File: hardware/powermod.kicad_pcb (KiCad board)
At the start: 4 copper layers, 65 x 40 mm, 77 parts, among them J1 USB_C_IN, J2 USB_C_OUT, J3 JST_PH_2, J4 STEMMA_QT, J5 UPDI_HDR, Q1 AON7407, Q2 AON7407, Q3 BSS138, SW1 BUTTON, U1 BM8563, U2 ATtiny1616, U3 TPS63020DSJR, U4 TP4056, U5 XC6206P332MR, Y1 32.768kHz

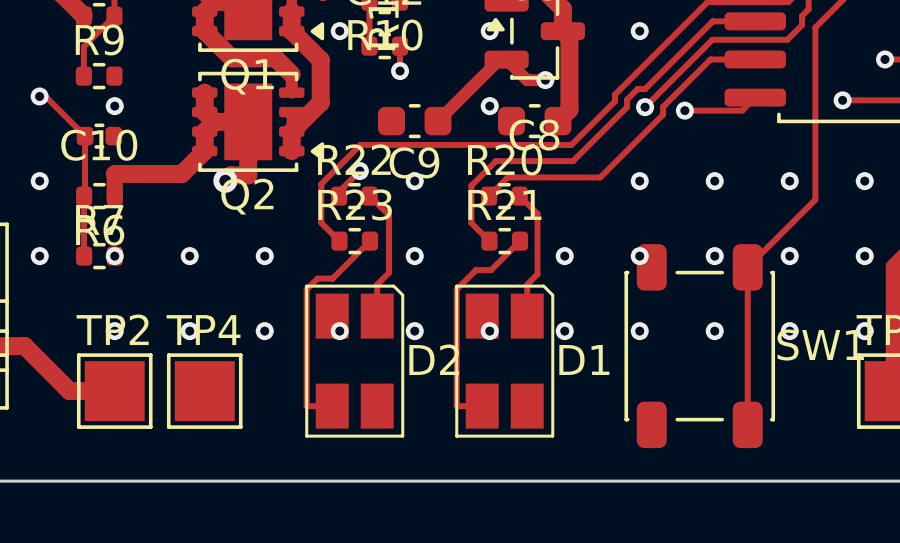
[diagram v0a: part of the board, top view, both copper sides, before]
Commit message: hardware: commit LED + crystal BOM parts (both in-stock, verified)
Crystal Y1: Epson Q13FC13500004 (LCSC C32346, ~286k stock) — 32.768kHz
CL=12.5pF matching the BM8563. Netlist-only (footprint unchanged).

LEDs D1/D2: TOGIALED TJ-S3227 (LCSC C601677, ~7.7k stock), yellow-green die
fixes the dim-green issue. Its pinout is the OPPOSITE numbering to the stock
KiCad Avago PLCC4 (would reverse polarity), so a local footprint was built
from LCSC's EasyEDA model (2 independent diodes, anodes=pins 2/3,
cathodes=pins 1/4). D1/D2 swapped on the board and anodes re-routed; cathodes
tie through the GND pour. Board rebuilt at rot 0 (anodes stacked under the
resistors, no crossing). LED_SMD lib dropped (both LEDs now in powermod lib).

Verified: pad-diff 214/214 + 11 NC, 0 unconnected, 0 clearance, only the 4
intrinsic U3 QFN-neck track_width flags. Red/green die identity is
firmware-adjustable (documented in PREFAB_AUDIT.md).

Co-Authored-By: Claude Opus 4.8 <noreply@anthropic.com>
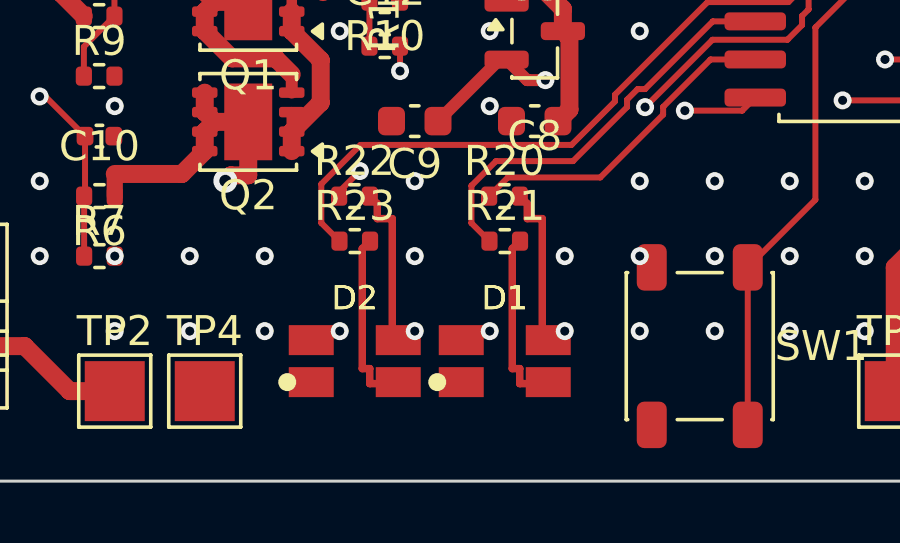
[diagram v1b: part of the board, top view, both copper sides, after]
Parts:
- D1, D2: value LED_RG_PLCC4 -> TJ-S3227; footprint LED_Avago_PLCC4_3.2x2.8mm_CW -> LED_TJ-S3227_RG_3.2x2.7mm
- turned D1 to 0 degrees
- turned D2 to 0 degrees
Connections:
- D1 pad 1: D1_RED -> GND
- D1 pad 2: GND -> D1_GRN
- D1 pad 3: D1_GRN -> D1_RED
- D2 pad 1: D2_RED -> GND
- D2 pad 2: GND -> D2_GRN
- D2 pad 3: D2_GRN -> D2_RED
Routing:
- net D2_GRN: track 7.52 -> 6.18 mm
- net D1_GRN: track 7.52 -> 6.18 mm
- net D1_RED: track 4.39 -> 5.67 mm, vias 0 -> 1
- net D2_RED: track 4.43 -> 5.67 mm, vias 0 -> 1
- net GND: vias 151 -> 149

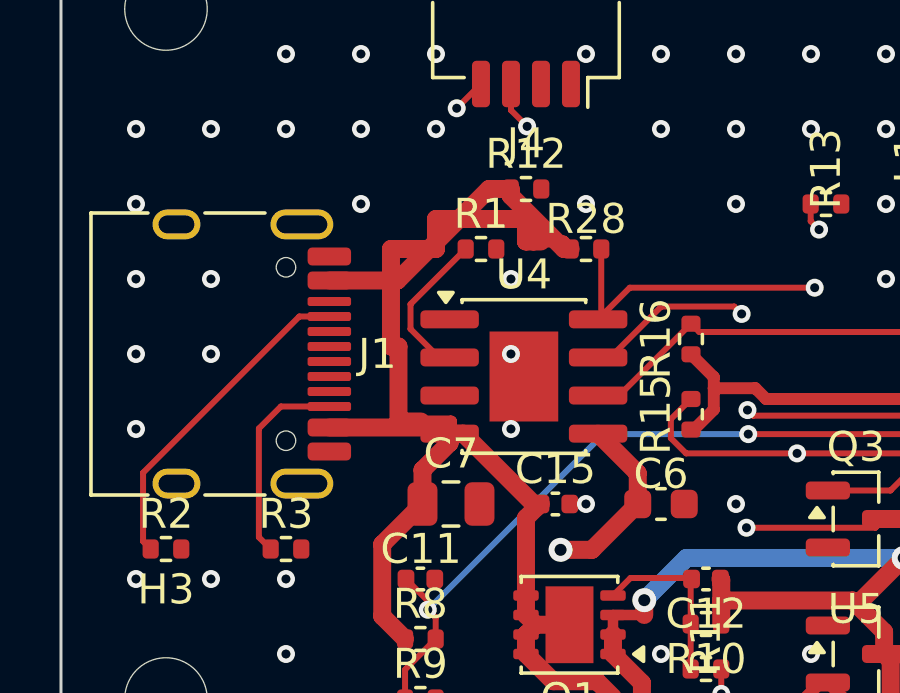
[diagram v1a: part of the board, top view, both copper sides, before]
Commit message: hardware: VBUS current-sharing (manual route) + audit review pass
VBUS current-sharing (audit open item d): A4↔A9 tied with a 0.6mm F.Cu link
in the narrow channel right of the connector pad column — routed by hand in
KiCad where the scripts could only fit 0.4mm. Split is now A9 73% / A4 27%
(was ~100/0): A9's USB-C contacts drop from 1.15A to 0.84A each at the 2.3A
peak, comfortably inside the ~1.25A/contact rating. Also simplified several
VBUS/other routes in passing.

Audit review pass on PREFAB_AUDIT.md: fixed stale counts (214/214 pads, 234
SMD pads); rewrote the ADC-reference firmware note (use VDD/3.3V or 2.5V, not
the marginal 1.5V); added Finding 3 (power-rail width-vs-current analysis) and
the U3 EP via-tenting fab note.

Verified: pad-diff 214/214 + 11 NC, 0 unconnected, 0 clearance, all rails at
spec (only the 4 intrinsic U3 QFN-neck track_width flags).

Co-Authored-By: Claude Opus 4.8 <noreply@anthropic.com>
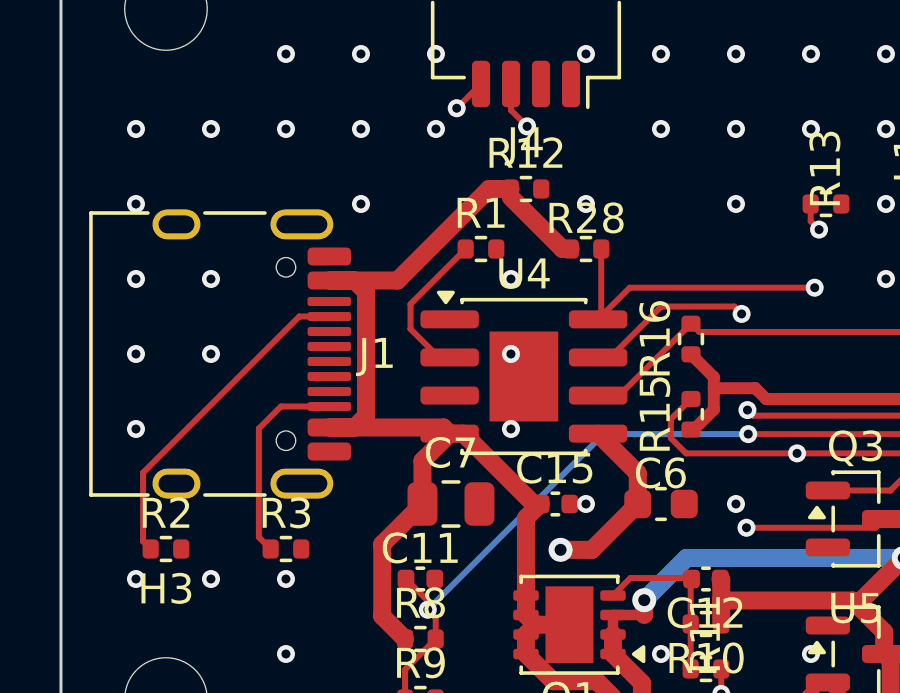
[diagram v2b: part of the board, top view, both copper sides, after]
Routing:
- net VBUS: track 53.3 -> 43.8 mm
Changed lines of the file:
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@@
-	)
-	(segment
-		(start 12.5 11.5)
-		(end 12.5 10.5)
-		(width 0.6)
-		(layer "F.Cu")
-		(net "VBUS")
-	)
-	(segment
-		(start 15.75 11.25)
-		(end 16 11.25)
-		(width 0.6)
-		(layer "F.Cu")
-		(net "VBUS")
-	)
-	(segment
-		(start 12 17.25)
-		(end 11.25 17.25)
-		(width 0.6)
-		(layer "F.Cu")
-		(net "VBUS")
 	)
 	(segment
@@
 	)
 	(segment
-		(start 16.75 11.25)
-		(end 16.99 11.5)
-		(width 0.4)
-		(layer "F.Cu")
-		(net "VBUS")
-	)
-	(segment
-		(start 15.5 10.5)
-		(end 15.5 11.25)
-		(width 0.6)
-		(layer "F.Cu")
-		(net "VBUS")
-	)
-	(segment
-		(start 16 11.25)
-		(end 16.75 11.25)
-		(width 0.4)
-		(layer "F.Cu")
-		(net "VBUS")
-	)
-	(segment
-		(start 12.955 17.655)
-		(end 12.955 17.9616)
-		(width 0.6)
-		(layer "F.Cu")
-		(net "VBUS")
-	)
-	(segment
 		(start 16.4083 25.9083)
 		(end 15.5 25)
@@
 	)
 	(segment
-		(start 12.5 10.5)
-		(end 15.5 10.5)
-		(width 0.6)
-		(layer "F.Cu")
-		(net "VBUS")
-	)
-	(segment
 		(start 15.825 24.025)
 		(end 15.5 23.7)
@@
 	)
 	(segment
-		(start 11 14.75)
-		(end 11 11.5)
-		(width 0.6)
-		(layer "F.Cu")
-		(net "VBUS")
-	)
-	(segment
 		(start 15.862 20.1032)
 		(end 15.9652 20)
@@
 	)
 	(segment
-		(start 13 17.25)
-		(end 12 17.25)
-		(width 0.4)
-		(layer "F.Cu")
-		(net "VBUS")
-	)
-	(segment
-		(start 11.25 14.75)
-		(end 11 14.75)
+		(start 9.785252 12.55)
+		(end 10.17 12.934748)
+		(width 0.6)
+		(layer "F.Cu")
+		(net "VBUS")
+	)
+	(segment
+		(start 12.05 18.56)
+		(end 12.955 17.655)
+		(width 0.6)
+		(layer "F.Cu")
+		(net "VBUS")
+	)
+	(segment
+		(start 16.99 11.5)
+		(end 16.720001 11.5)
 		(width 0.6)
 		(layer "F.Cu")
@@
 	)
 	(segment
+		(start 9.785252 17.45)
+		(end 8.945 17.45)
+		(width 0.6)
+		(layer "F.Cu")
+		(net "VBUS")
+	)
+	(segment
 		(start 14.268232 9.5)
 		(end 14.99 9.5)
@@
 	)
 	(segment
+		(start 10.17 17.065252)
+		(end 9.785252 17.45)
+		(width 0.6)
+		(layer "F.Cu")
+		(net "VBUS")
+	)
+	(segment
 		(start 11.218232 12.55)
 		(end 14.268232 9.5)
@@
 	)
 	(segment
+		(start 16.720001 11.5)
+		(end 14.99 9.769999)
+		(width 0.6)
+		(layer "F.Cu")
+		(net "VBUS")
+	)
+	(segment
+		(start 12.05 20)
+		(end 12.05 18.56)
+		(width 0.6)
+		(layer "F.Cu")
+		(net "VBUS")
+	)
+	(segment
 		(start 13.4138 17.655)
 		(end 12.955 17.655)
@@
 	)
 	(segment
-		(start 16.7667 11.5)
-		(end 14.99 9.7233)
-		(width 0.6)
-		(layer "F.Cu")
-		(net "VBUS")
-	)
-	(segment
-		(start 13 17.75)
-		(end 13 17.25)
-		(width 0.4)
-		(layer "F.Cu")
-		(net "VBUS")
-	)
-	(segment
 		(start 11.47 24.5)
 		(end 10.7074 23.7374)
@@
 	)
 	(segment
-		(start 11.25 17.25)
-		(end 11.25 14.75)
-		(width 0.6)
-		(layer "F.Cu")
-		(net "VBUS")
-	)
-	(segment
 		(start 8.945 17.45)
 		(end 12.75 17.45)
@@
 		(start 8.945 12.55)
 		(end 11.218232 12.55)
-		(width 0.6)
-		(layer "F.Cu")
-		(net "VBUS")
-	)
-	(segment
-		(start 14.99 9.7233)
-		(end 14.99 9.5)
 		(width 0.6)
 		(layer "F.Cu")
@@
 	)
 	(segment
-		(start 16.99 11.5)
-		(end 16.7667 11.5)
-		(width 0.6)
-		(layer "F.Cu")
-		(net "VBUS")
-	)
-	(segment
-		(start 11 11.5)
-		(end 12.5 11.5)
+		(start 10.17 12.934748)
+		(end 10.17 17.065252)
 		(width 0.6)
 		(layer "F.Cu")
@@
 	)
 	(segment
-		(start 12.955 17.9616)
-		(end 12.05 18.8666)
+		(start 8.945 12.55)
+		(end 9.785252 12.55)
 		(width 0.6)
 		(layer "F.Cu")
@@
 		(start 10.7074 23.7374)
 		(end 10.7074 21.3426)
-		(width 0.6)
-		(layer "F.Cu")
-		(net "VBUS")
-	)
-	(segment
-		(start 15.5 11.25)
-		(end 15.75 11.25)
-		(width 0.6)
-		(layer "F.Cu")
-		(net "VBUS")
-	)
-	(segment
-		(start 12.96 17.66)
-		(end 13 17.75)
-		(width 0.4)
-		(layer "F.Cu")
-		(net "VBUS")
-	)
-	(segment
-		(start 12.05 18.8666)
-		(end 12.05 20)
 		(width 0.6)
 		(layer "F.Cu")
@@
 	)
 	(segment
+		(start 21 36.25)
+		(end 20.75 36.25)
+		(width 0.25)
+		(layer "F.Cu")
+		(net "D2_GRN")
+	)
+	(segment
+		(start 22 36.75)
+		(end 21 36.75)
+		(width 0.25)
+		(layer "F.Cu")
+		(net "D2_GRN")
+	)
+	(segment
+		(start 20.75 32.25)
+		(end 21.01 32)
+		(width 0.25)
+		(layer "F.Cu")
+		(net "D2_GRN")
+	)
+	(segment
+		(start 21 36.75)
+		(end 21 36.25)
+		(width 0.25)
+		(layer "F.Cu")
+		(net "D2_GRN")
+	)
+	(segment
+		(start 20.75 36.25)
+		(end 20.75 32.25)
+		(width 0.25)
+		(layer "F.Cu")
+		(net "D2_GRN")
+	)
+	(segment
+		(start 21.95 36.7)
+		(end 22 36.75)
+		(width 0.25)
+		(layer "F.Cu")
+		(net "D2_GRN")
+	)
+	(segment
 		(start 25.6022 29.8778)
 		(end 28.6848 29.8778)
@@
 		(net "Q3_DRAIN")
 	)
-	(segment
-		(start 21 36.25)
-		(end 20.75 36.25)
-		(width 0.25)
-		(layer "F.Cu")
-		(net "D2_GRN")
-	)
-	(segment
-		(start 22 36.75)
-		(end 21 36.75)
-		(width 0.25)
-		(layer "F.Cu")
-		(net "D2_GRN")
-	)
-	(segment
-		(start 20.75 32.25)
-		(end 21.01 32)
-		(width 0.25)
-		(layer "F.Cu")
-		(net "D2_GRN")
-	)
-	(segment
-		(start 21 36.75)
-		(end 21 36.25)
-		(width 0.25)
-		(layer "F.Cu")
-		(net "D2_GRN")
-	)
-	(segment
-		(start 20.75 36.25)
-		(end 20.75 32.25)
-		(width 0.25)
-		(layer "F.Cu")
-		(net "D2_GRN")
-	)
-	(segment
-		(start 21.95 36.7)
-		(end 22 36.75)
-		(width 0.25)
-		(layer "F.Cu")
-		(net "D2_GRN")
-	)
 	(zone

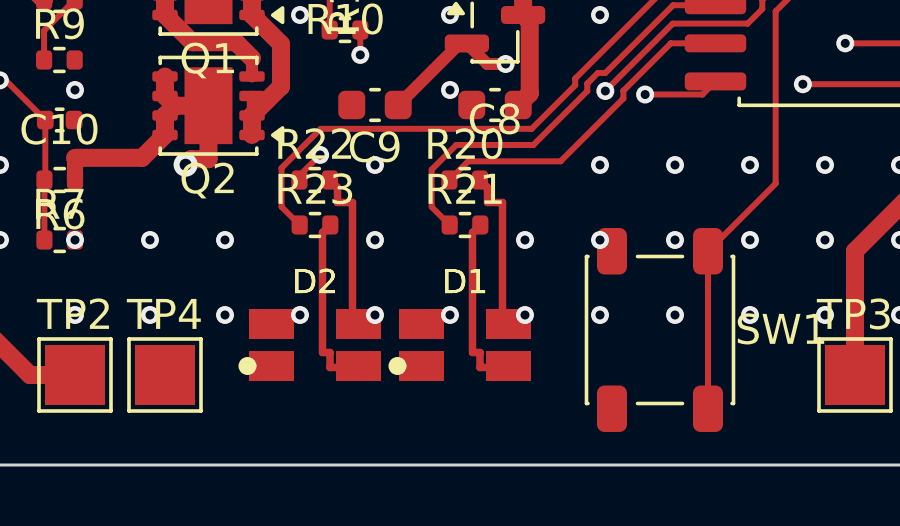
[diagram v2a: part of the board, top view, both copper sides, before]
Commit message: hardware: gerber review — remove 2 dangling vias on D1_RED/D2_RED
Fab-review pass: exported full gerber+drill set and checked manufacturing
minimums (all inside JLCPCB standard: 0.2mm trace/space, 0.6/0.3 vias =
0.15mm ring, 0.3mm min drill, 0.225mm min PTH ring). DRC clean except
cosmetic silk + the 4 intrinsic U3 QFN necks.

Found and removed 2 dangling vias (redundant single-layer stubs on the LED
red-anode nets at (22.5,35)/(27.5,35)) left over from LED-area routing.
Verified: 0 unconnected, pad-diff still 214/214.

Co-Authored-By: Claude Opus 4.8 <noreply@anthropic.com>
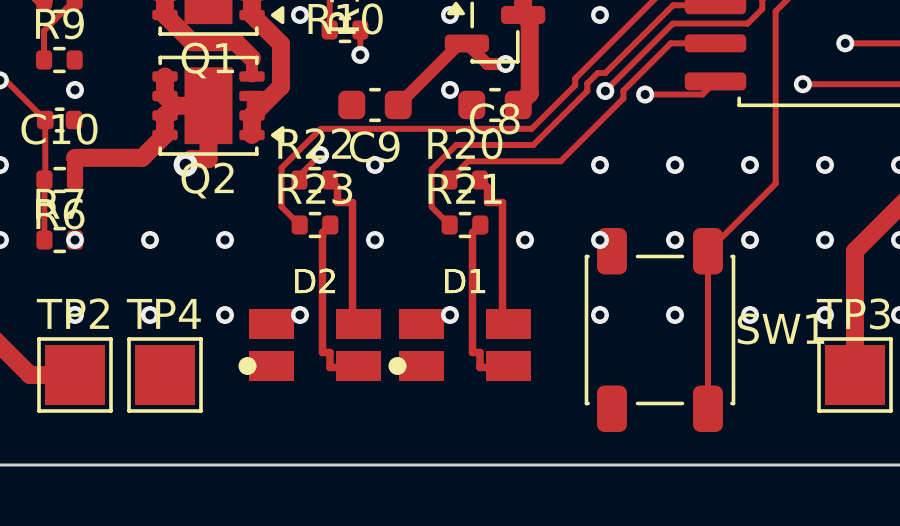
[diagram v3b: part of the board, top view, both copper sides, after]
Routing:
- net D2_RED: vias 1 -> 0
- net D1_RED: vias 1 -> 0
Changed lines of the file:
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@@
-		(net "D2_RED")
-	)
-	(via
-		(at 22.5 35)
-		(size 0.6)
-		(drill 0.3)
-		(layers "F.Cu" "B.Cu")
 		(net "D2_RED")
 	)
@@
 		(net "D1_RED")
 	)
-	(via
-		(at 27.5 35)
-		(size 0.6)
-		(drill 0.3)
-		(layers "F.Cu" "B.Cu")
-		(net "D1_RED")
-	)

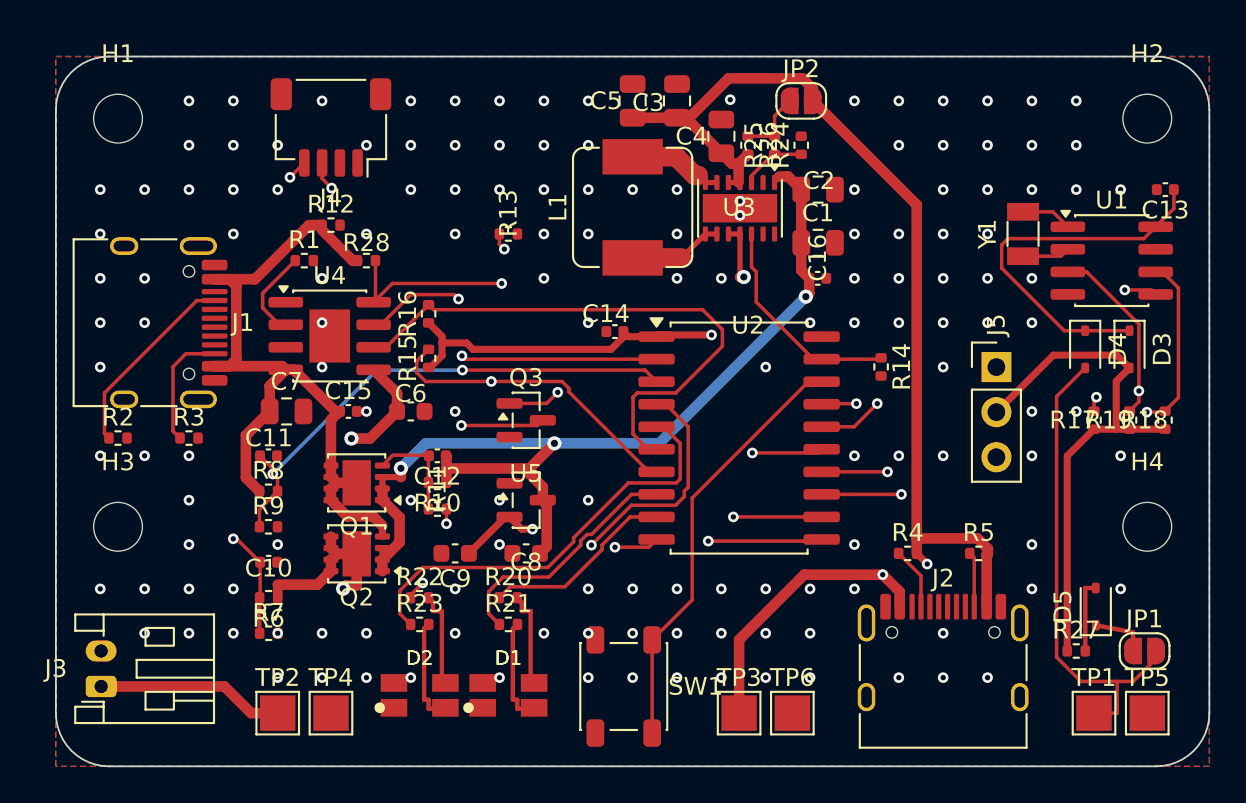
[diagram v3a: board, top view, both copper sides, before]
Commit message: hardware: board footprint swap for PY32F003 (U2 TSSOP-20, J5 SWD, TP7 NRST)
Text-level swap on powermod.kicad_pcb (pcbnew footprint mutation segfaults):
- U2 SOIC-20W -> TSSOP-20_4.4x6.5mm, 20 pads net-assigned to the PY32 pinmap
- J5 3-pin UPDI -> 3-pin SWD (GND/SWCLK/SWDIO); a 5-pin header won't fit the
  packed RTC/USB corner, so NRST is exposed on the new TP7 probe pad instead
- stripped 201 stale MCU-net segments + 6 local 3V3/GND stubs
Verified in pcbnew: correct nets, zero courtyard collisions. DRC clean apart
from the 4 known U3 track_width necks + 36 unrouted MCU connections (ratsnest).
MCU-area routing still to do; power/USB/charger routing untouched.

Co-Authored-By: Claude Opus 4.8 <noreply@anthropic.com>
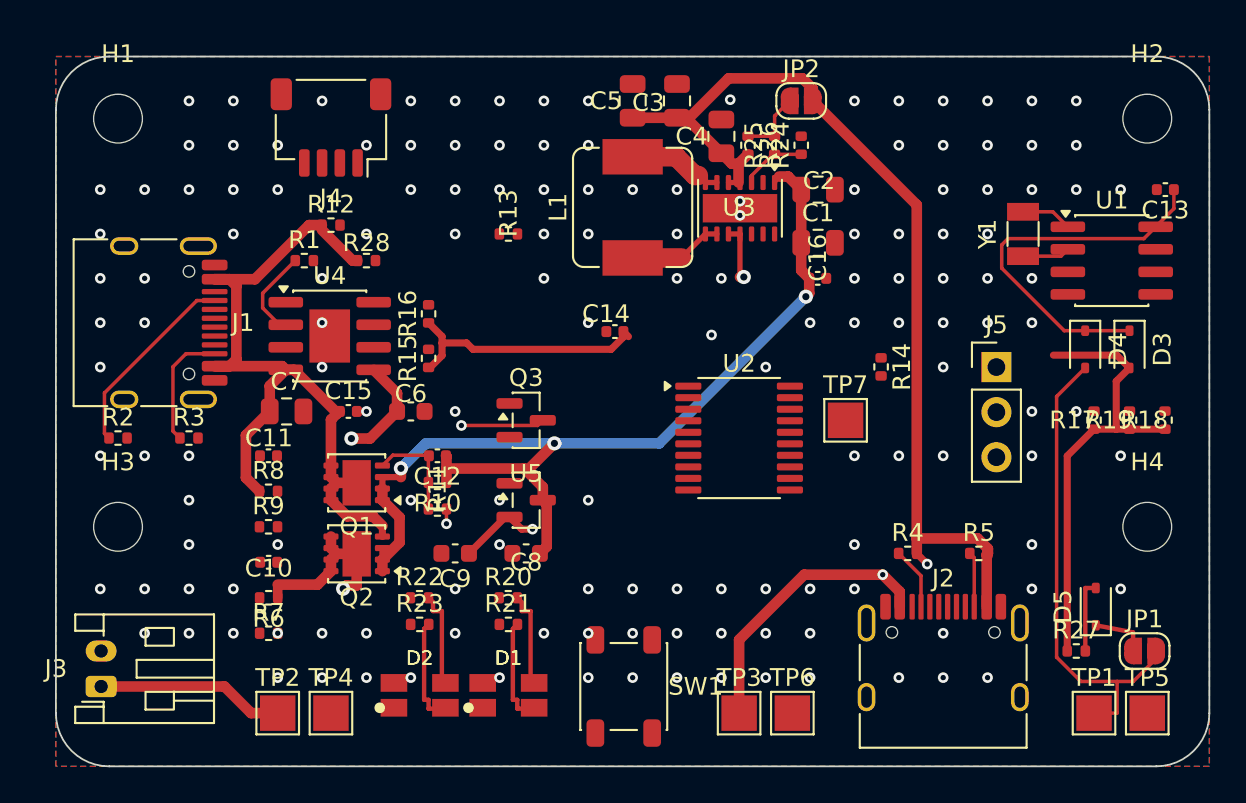
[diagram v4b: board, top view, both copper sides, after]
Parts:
- added TP7: NRST_PAD, TestPoint_Pad_2.0x2.0mm, F.Cu at (44.5, 20.5)
- J5: value UPDI_HDR -> SWD_HDR
- U2: value ATtiny1616 -> PY32F003F18P6; footprint SOIC-20W_7.5x12.8mm_P1.27mm -> TSSOP-20_4.4x6.5mm_P0.65mm
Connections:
- J5 pad 1: UPDI -> GND
- J5 pad 2: 3V3 -> LED_BAT_B
- J5 pad 3: GND -> LED_BAT_A
- U2 pad 1: 3V3 -> Q1_GATE_DRV
- U2 pad 10: SDA -> LED_BAT_A
- U2 pad 11: SCL -> LED_BAT_B
- U2 pad 12: CHG_CE -> CHG_CHRG
- U2 pad 13: RTC_SCL -> SCL
- U2 pad 14: RTC_INT -> SDA
- U2 pad 15: Q1_GATE_DRV -> LED_PWR_B
- U2 pad 16: UPDI -> RTC_SDA
- U2 pad 17: RTC_SDA -> RTC_SCL
- U2 pad 18: BUTTON -> NRST
- U2 pad 19: CONV_EN -> LED_PWR_A
- U2 pad 2: VBAT_DIV -> CONV_EN
- U2 pad 20: GND -> BUTTON
- U2 pad 3: VBUS_DIV -> VBAT_DIV
- U2 pad 4: LED_BAT_A -> VBUS_DIV
- U2 pad 5: LED_BAT_B -> CHG_CE
- U2 pad 7: CHG_CHRG -> GND
- U2 pad 8: LED_PWR_B -> RTC_INT
- U2 pad 9: LED_PWR_A -> 3V3
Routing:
- net VBAT_DIV: track 53.2 -> 0.00 mm, vias 2 -> 0
- net SCL: track 40.8 -> 0.00 mm, vias 2 -> 0
- net Q1_GATE_DRV: track 36.6 -> 0.00 mm, vias 3 -> 0
- net CHG_CE: track 33.6 -> 0.00 mm, vias 2 -> 0
- net CHG_STDBY: track 32.2 -> 0.00 mm
- net SDA: track 31.0 -> 0.00 mm, vias 2 -> 0
- net RTC_INT: track 30.4 -> 0.00 mm, vias 2 -> 0
- net RTC_SCL: track 30.2 -> 0.00 mm, vias 2 -> 0
- net VBUS_DIV: track 29.2 -> 0.00 mm, vias 2 -> 0
- net CHG_CHRG: track 28.5 -> 0.00 mm, vias 2 -> 0
- net RTC_SDA: track 26.2 -> 0.00 mm, vias 3 -> 0
- net LED_BAT_A: track 25.5 -> 0.00 mm, vias 2 -> 0
- net LED_BAT_B: track 24.4 -> 0.00 mm
- net BUTTON: track 24.2 -> 0.00 mm
- net 3V3: track 93.0 -> 70.6 mm
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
